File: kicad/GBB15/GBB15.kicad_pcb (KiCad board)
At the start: 4 copper layers, 67 x 15 mm, 70 parts, among them J1 CAN_IN, J10 USB_C_Receptacle_USB2.0, J2 CAN_OUT, J3 M0_THERM, J4 M1_THERM, J5 Conn_01x04_Male, J6 Conn_01x04_Male, J7 ENDSTOP1, J8 ENDSTOP2, SW1 SW_Push, SW2 SW_Push, U1 TMC2209-LA-T, U2 STM32G0B1CEU6, U3 TMC2209-LA-T, U4 TCAN334, U5 NCP730BMT330TBG, Y1 Crystal_GND24

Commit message: Minor touches
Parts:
- moved R14 0.40 mm to (148.7, 85.5)
- moved C26 0.10 mm to (154.4, 98.6)
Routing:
- net GND: track 82.4 -> 80.4 mm, vias 125 -> 126
- net /CANH: track 32.4 -> 31.6 mm
- net +3V3: track 37.8 -> 37.0 mm
- net /MB_ENN: track 50.0 -> 50.6 mm
- net /MA_DIR: track 26.3 -> 25.8 mm

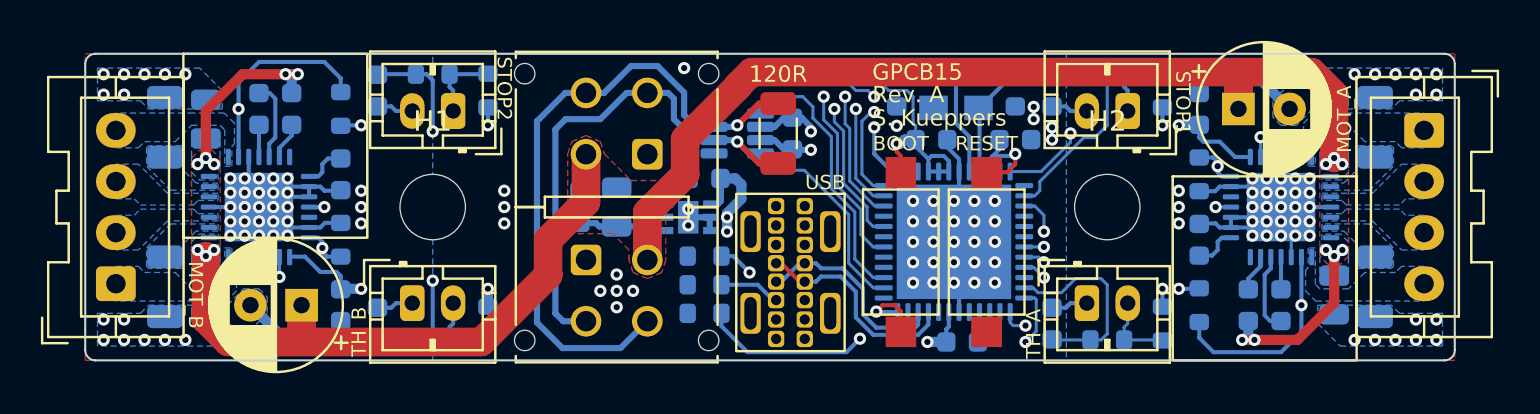
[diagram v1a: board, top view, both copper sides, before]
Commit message: Small changes in JST connector type
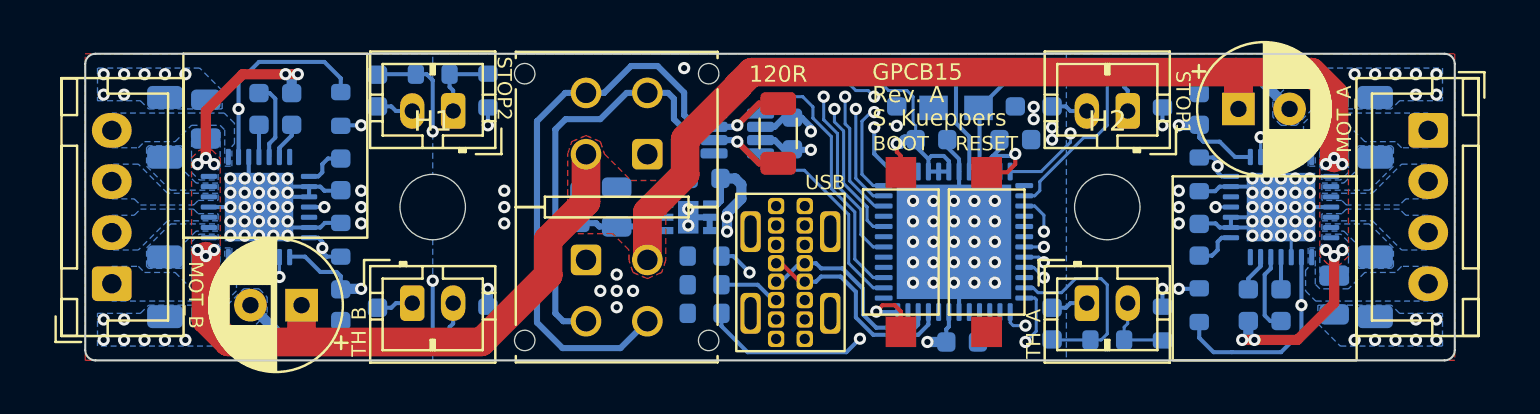
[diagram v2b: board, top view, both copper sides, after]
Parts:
- J5, J6: footprint Connector_JST:JST_XA_B04B-XASK-1_1x04_P2.50mm_Vertical -> Connector_JST:JST_XH_B4B-XH-A_1x04_P2.50mm_Vertical
- moved J6 0.20 mm to (112.8, 95.8)
- moved J5 0.20 mm to (177.2, 88.2)

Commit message: Connected unconnected pads on TCAN334 to ground
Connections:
- U4 pad 5: unconnected-(U4-Pad5) -> GND
- U4 pad 8: unconnected-(U4-Pad8) -> GND

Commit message: Correct 100nF capacitor part number and changed to MAX3051 instead of TCAN334
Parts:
- U4: value TCAN334 -> MAX3051EKA+T

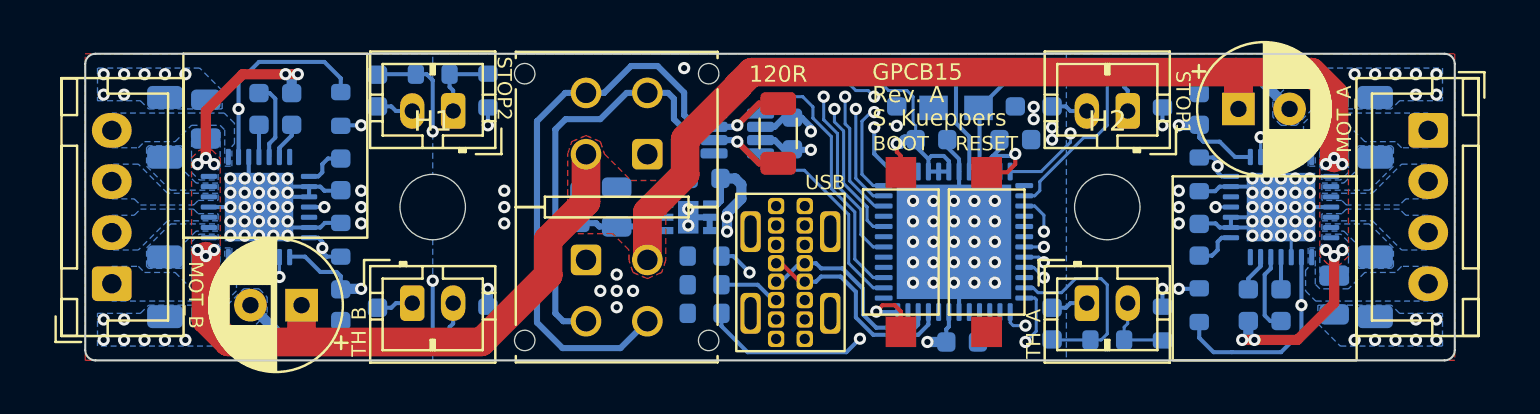
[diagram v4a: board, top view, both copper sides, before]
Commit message: Added tooling holes
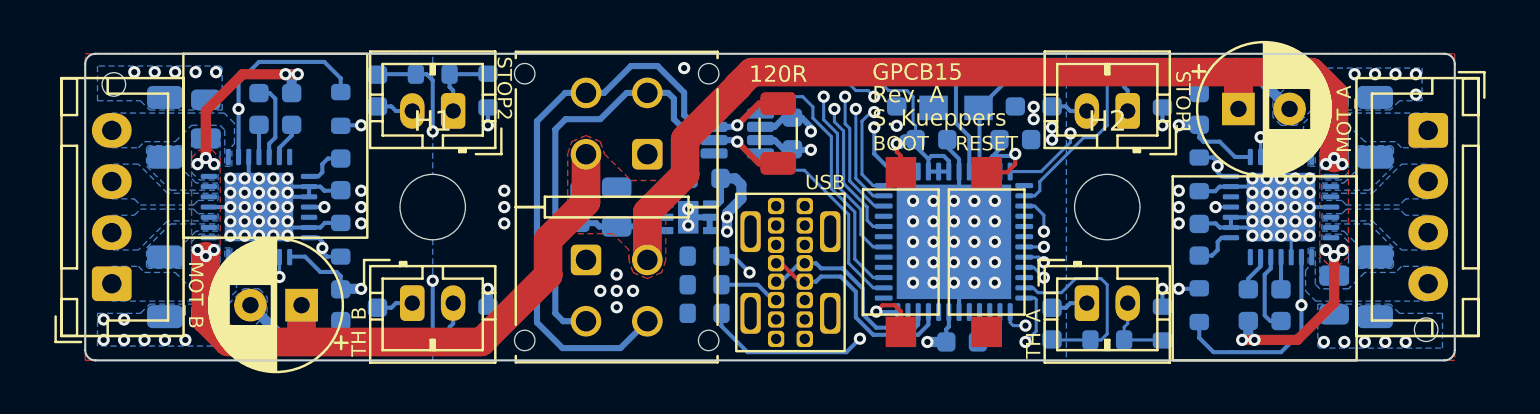
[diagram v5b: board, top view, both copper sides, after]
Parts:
- added FID1: Fiducial, Project:TOOLING-HOLE, F.Cu at (177.1, 98.0)
- added FID2: Fiducial, Project:TOOLING-HOLE, F.Cu at (112.9, 86.0)
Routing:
- net GND: vias 126 -> 120

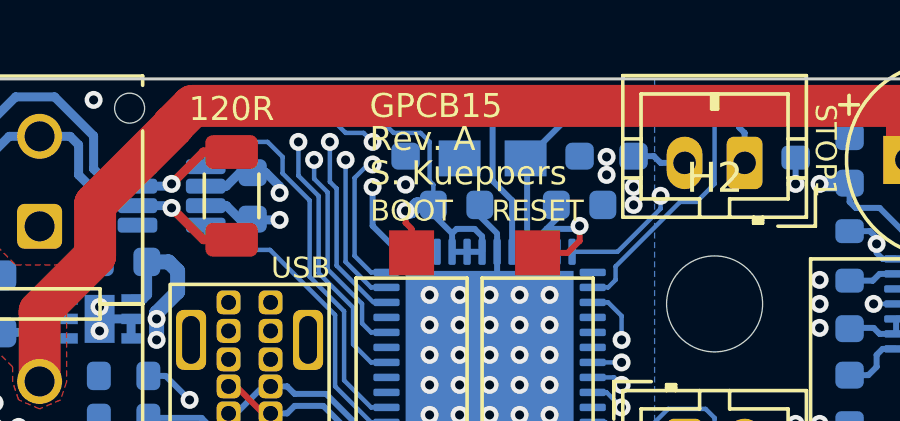
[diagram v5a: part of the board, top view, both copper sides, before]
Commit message: Changed silkscreen
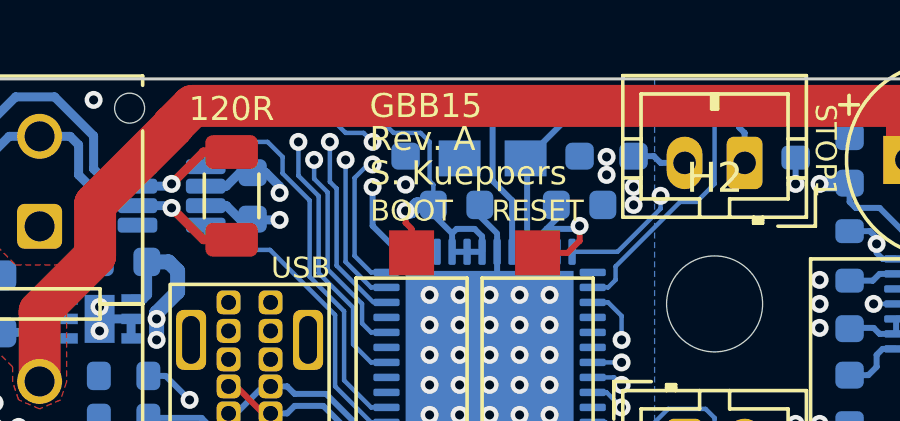
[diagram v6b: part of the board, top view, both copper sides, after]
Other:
- board text added: "GBB15"
- board text removed: "GPCB15"
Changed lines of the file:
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@@
     (effects (font (size 0.7 0.7) (thickness 0.15)))
   )
-  (gr_text "GPCB15\n" (at 150 85.4) (layer "F.SilkS")
+  (gr_text "GBB15\n" (at 150 85.4) (layer "F.SilkS")
     (effects (font (size 0.8 0.8) (thickness 0.15)) (justify left))
   )

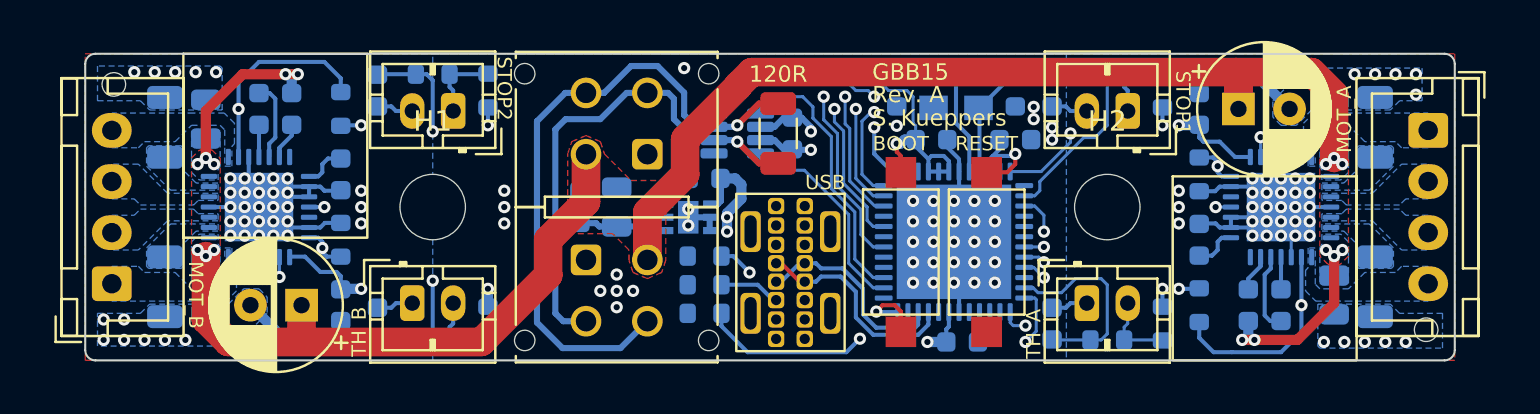
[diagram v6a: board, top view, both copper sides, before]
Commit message: Bumped revision to B, added Power LED and moved ENDSTOP2 to ADC pin
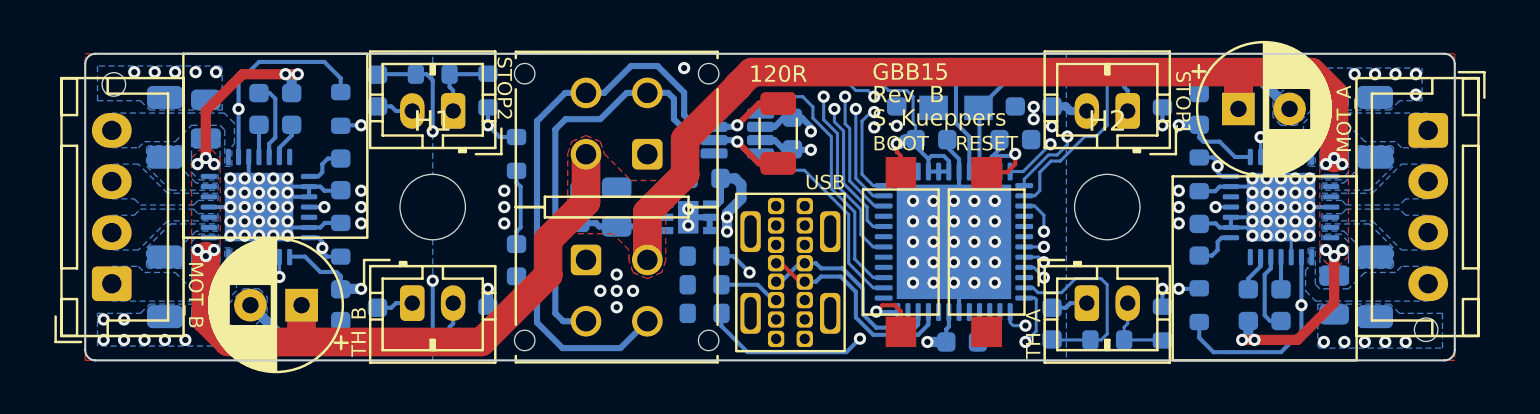
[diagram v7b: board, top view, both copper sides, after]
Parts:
- added D1: LED, LED_SMD:LED_0603_1608Metric, B.Cu at (132.6, 94.6)
- added R17: 4.7K, Resistor_SMD:R_0603_1608Metric, B.Cu at (132.6, 89.4)
- J3: value M0_THERM -> MA_THERM
- J4: value M1_THERM -> MB_THERM
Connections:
- net /ENDSTOP1 renamed /STOP1/TH1
- C28 pad 2: /ENDSTOP2 -> /STOP2/TH2
- R21 pad 1: /ENDSTOP2 -> /STOP2/TH2
- U2 pad 1: /ENDSTOP2 -> unconnected-(U2-Pad1)
- U2 pad 13: unconnected-(U2-Pad13) -> /STOP2/TH2
- U5 pad 5: unconnected-(U5-Pad5) -> GND
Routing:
- net /STOP2/TH2: track 0.00 -> 52.7 mm, vias 0 -> 3
- net /ENDSTOP2: track 37.1 -> 0.00 mm, vias 2 -> 0
- net Net-(D1-Pad2): track 0.00 -> 3.75 mm
- net /CHAM_THERM: track 26.2 -> 23.3 mm
- net +3V3: track 37.0 -> 38.7 mm
- net GND: vias 120 -> 119
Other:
- board text added: "Rev. B"
- board text removed: "Rev. A"

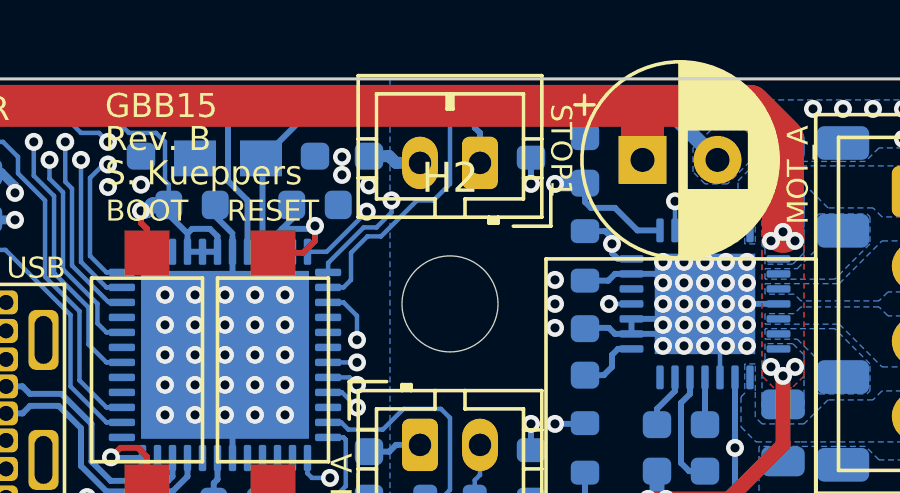
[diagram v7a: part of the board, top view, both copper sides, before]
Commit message: Added pinout documentation on User.Drawings layer
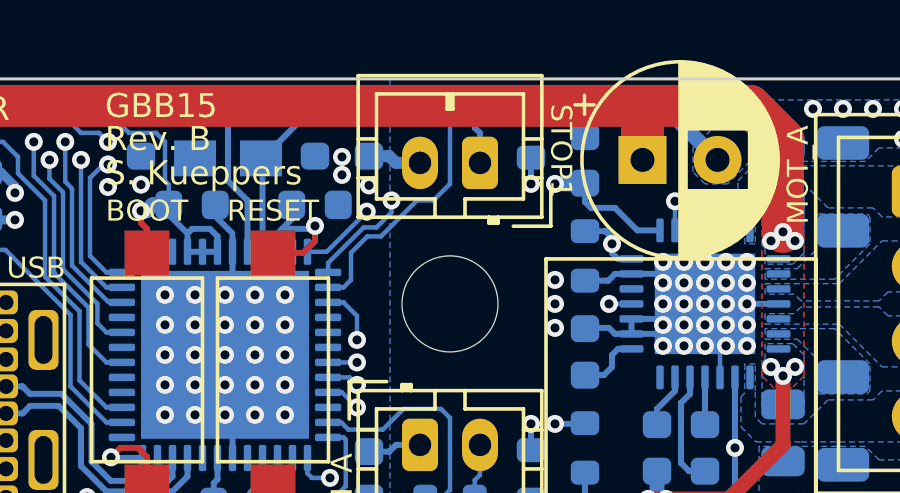
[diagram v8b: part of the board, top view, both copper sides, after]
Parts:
- J10: value USB_C_Receptacle_USB2.0 -> USB-C
- J5: value Conn_01x04_Male -> MA
- J6: value Conn_01x04_Male -> MB
- SW1: value SW_Push -> BOOT
- SW2: value SW_Push -> RESET
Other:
- board text added: "24V"
- board text added: "CANH"
- board text added: "CANL"
- board text added: "CHAMB_THERM"
- board text added: "GND"
- board text added: "MA_A1"
- board text added: "MA_A2"
- board text added: "MA_B1"
- board text added: "MA_B2"
- board text added: "MB_A1"
- board text added: "MB_A2"
- board text added: "MB_B1"
- board text added: "MB_B2"
